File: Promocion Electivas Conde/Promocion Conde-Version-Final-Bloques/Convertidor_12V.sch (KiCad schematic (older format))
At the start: 3 parts, among them J1 Bornera continua > 15V

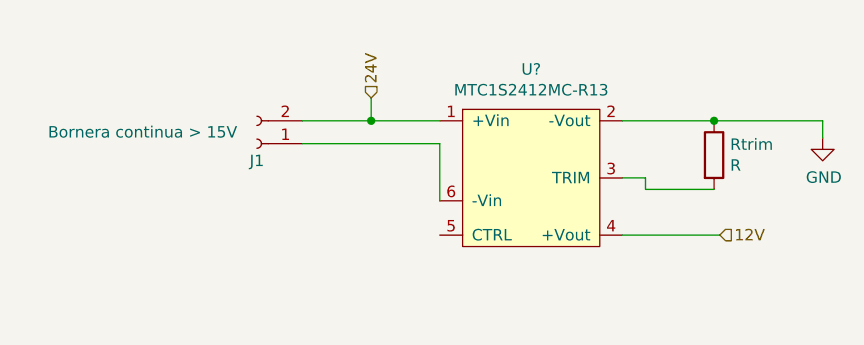
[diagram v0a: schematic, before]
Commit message: Actualizacion
Actualizo los footprints del esquematico y se inicia el PCB
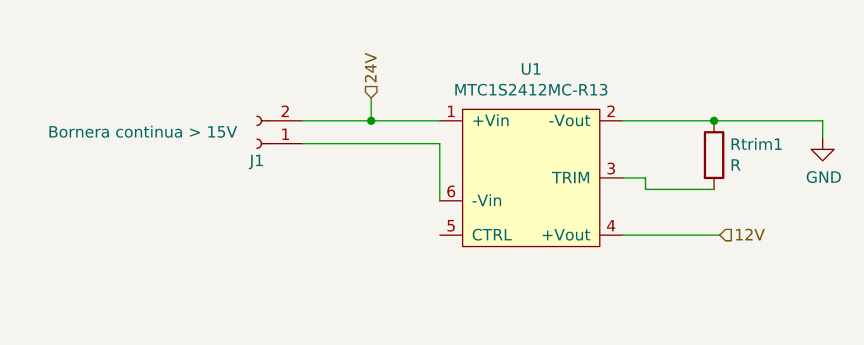
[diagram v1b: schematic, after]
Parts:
- Rtrim1: renamed from Rtrim; footprint (none) -> Resistor_SMD:R_0201_0603Metric_Pad0.64x0.40mm_HandSolder
- gave numbers to parts that had none: 1
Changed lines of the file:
@@
 24V
 $Comp
-L Converter_DCDC:MTC1S2412MC-R13 U?
+L Converter_DCDC:MTC1S2412MC-R13 U1
 U 1 1 618D6B55
 P 5675 2650
-F 0 "U?" H 5675 3125 50  0000 C CNN
+F 0 "U1" H 5675 3125 50  0000 C CNN
 F 1 "MTC1S2412MC-R13" H 5675 3034 50  0000 C CNN
 F 2 "Converter_DCDC:MTC1S2412MC-R13" H 5725 3350 50  0001 C CNN
@@
 $EndComp
 $Comp
-L Device:R Rtrim
+L Device:R Rtrim1
 U 1 1 618DFED1
 P 6475 2550
-F 0 "Rtrim" H 6545 2596 50  0000 L CNN
+F 0 "Rtrim1" H 6545 2596 50  0000 L CNN
 F 1 "R" H 6545 2505 50  0000 L CNN
-F 2 "" V 6405 2550 50  0001 C CNN
+F 2 "Resistor_SMD:R_0201_0603Metric_Pad0.64x0.40mm_HandSolder" V 6405 2550 50  0001 C CNN
 F 3 "~" H 6475 2550 50  0001 C CNN
 	1    6475 2550

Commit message: Layers de 12V y 24V
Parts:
- U1: symbol Converter_DCDC:MTC1S2412MC-R13 -> Conversor-rescue:MTC1S2412MC-R13-Converter_DCDC
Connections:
- net 12V renamed +12V
- net 24V renamed +24V
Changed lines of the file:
@@
 24V
 $Comp
-L Converter_DCDC:MTC1S2412MC-R13 U1
+L Conversor-rescue:MTC1S2412MC-R13-Converter_DCDC U1
 U 1 1 618D6B55
 P 5675 2650
+AR Path="/618D6B55" Ref="U1"  Part="1"
+AR Path="/612E3FD7/618D6B55" Ref="U1"  Part="1"
 F 0 "U1" H 5675 3125 50  0000 C CNN
 F 1 "MTC1S2412MC-R13" H 5675 3034 50  0000 C CNN
@@
 	4975 2400 5275 2400
 Wire Wire Line
-	4675 2400 4975 2400
+	4675 2400 4825 2400
 Connection ~ 4975 2400
 Wire Wire Line
@@
 	6950 2400 6950 2475
 Wire Wire Line
-	6075 2900 6500 2900
+	6075 2900 6125 2900
 Wire Wire Line
 	6475 2400 6950 2400
 Connection ~ 6475 2400
+$Comp
+L power:+12V #PWR0112
+U 1 1 61A2B710
+P 6350 3225
+F 0 "#PWR0112" H 6350 3075 50  0001 C CNN
+F 1 "+12V" H 6365 3398 50  0000 C CNN
+F 2 "" H 6350 3225 50  0001 C CNN
+F 3 "" H 6350 3225 50  0001 C CNN
+	1    6350 3225
+	1    0    0    -1
+$EndComp
+Wire Wire Line
+	6350 3225 6350 3300
+Wire Wire Line
+	6350 3300 6125 3300
+Wire Wire Line
+	6125 3300 6125 2900
+Connection ~ 6125 2900
+Wire Wire Line
+	6125 2900 6500 2900
+$Comp
+L power:+24V #PWR?
+U 1 1 61A2D443
+P 4825 2175
+F 0 "#PWR?" H 4825 2025 50  0001 C CNN
+F 1 "+24V" H 4840 2348 50  0000 C CNN
+F 2 "" H 4825 2175 50  0001 C CNN
+F 3 "" H 4825 2175 50  0001 C CNN
+	1    4825 2175
+	1    0    0    -1
+$EndComp
+Wire Wire Line
+	4825 2175 4825 2400
+Connection ~ 4825 2400
+Wire Wire Line
+	4825 2400 4975 2400
 $EndSCHEMATC
